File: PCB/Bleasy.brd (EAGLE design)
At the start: 100 x 80 mm, 14 parts, among them IC1 ATMEGA328-PU, Q1 8 MHz

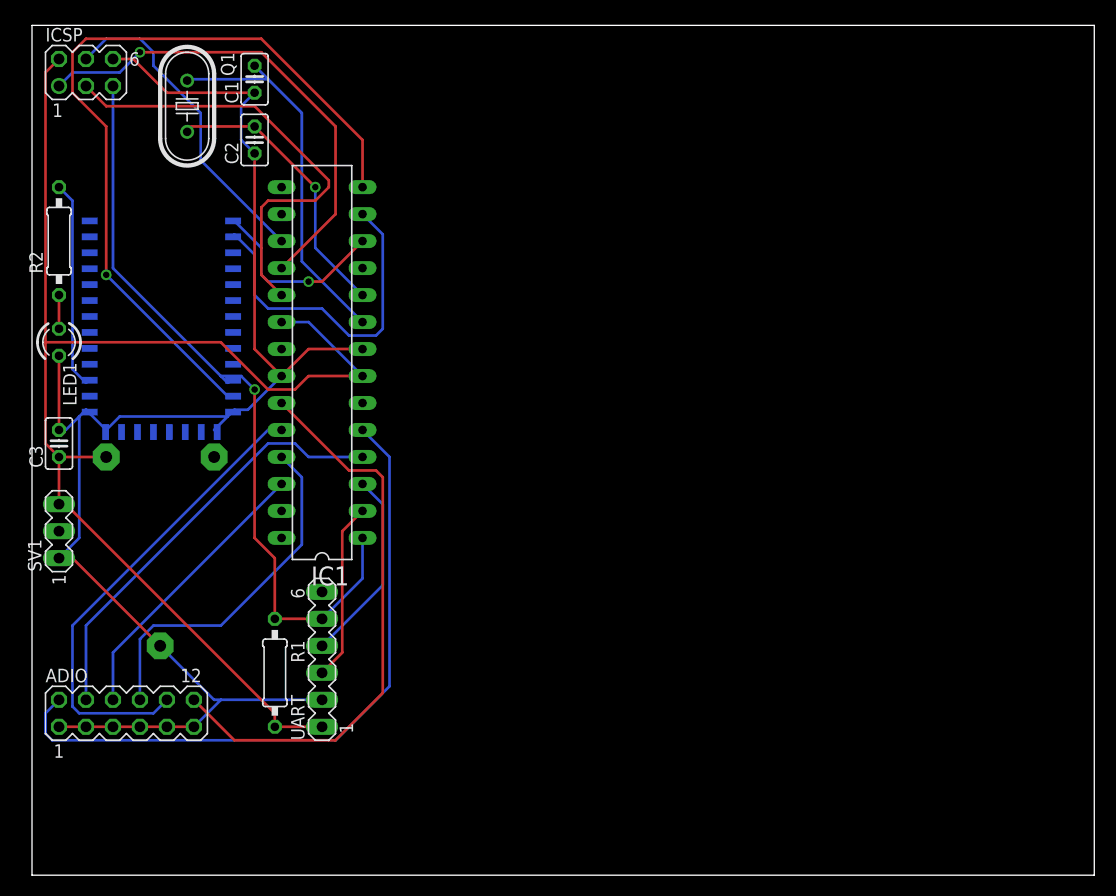
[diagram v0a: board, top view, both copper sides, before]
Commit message: New cell coin adapter
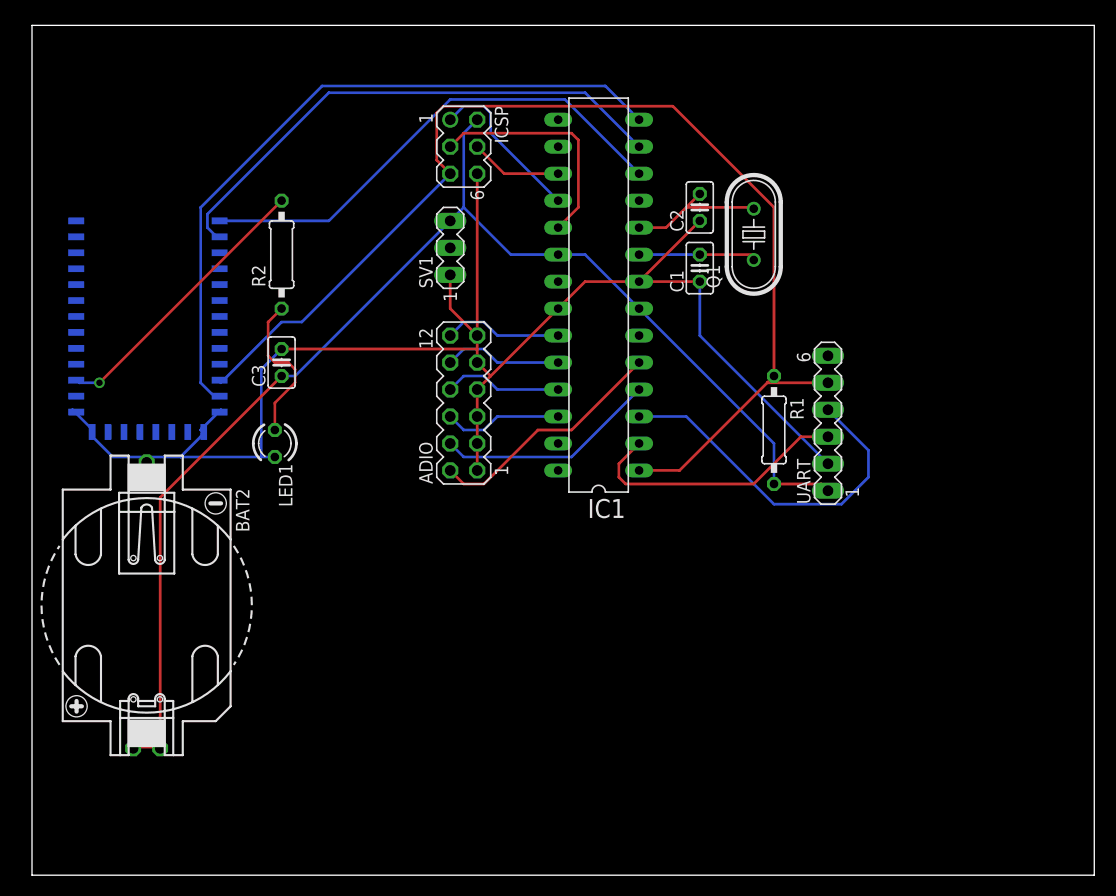
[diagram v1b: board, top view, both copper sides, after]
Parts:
- removed G1: CR2032H, battery:CR2032H
- added BAT2: CR2032_2+_1-SKT, con_bat_2032__s_:CR2032-SOCKET-THT
- moved Q1 54.7 mm to (67.9, 60.3), turned to 90 degrees
- moved UART 52.6 mm to (74.9, 42.5)
- moved R1 52.3 mm to (69.8, 41.9)
- moved C1 45.5 mm to (62.9, 57.1)
- moved SV1 45.5 mm to (39.4, 59.1)
- moved ADIO 43.1 mm to (40.6, 44.5), turned to 90 degrees
- moved C2 42.4 mm to (62.9, 62.9)
- moved ICSP 36.2 mm to (40.6, 68.6), turned to 270 degrees
- moved IC1 26.8 mm to (53.3, 54.6)
- moved LED1 22.4 mm to (22.9, 40.6)
- moved C3 22.3 mm to (23.5, 48.3)
- moved R2 21.0 mm to (23.5, 58.4)
- moved E1 1.27 mm to (10.2, 61.6)
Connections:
- net +3V3: now also BAT2.2, BAT2.3; no longer G1.+
- net GND: now also BAT2.1; no longer G1.-
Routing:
- net N$9: track 53.9 -> 11.2 mm
- net N$4: track 63.6 -> 23.0 mm
- net RST: track 72.7 -> 110.2 mm, vias 1 -> 0
- net N$10: track 44.6 -> 11.2 mm
- net MISO: track 45.7 -> 15.5 mm, vias 1 -> 0
- net HM10_TX: track 17.6 -> 47.1 mm, vias 1 -> 0
- net N$2: track 36.1 -> 11.3 mm
- net N$11: track 33.7 -> 11.2 mm
- net N$3: track 30.4 -> 8.67 mm
- net SCK: track 43.4 -> 21.9 mm
- net N$5: track 40.6 -> 20.9 mm
- net HM10_RX: track 32.3 -> 50.2 mm
- net N$12: track 26.9 -> 11.2 mm
- net TX: track 18.4 -> 34.0 mm
- net N$1: track 26.9 -> 13.5 mm, vias 1 -> 0
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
